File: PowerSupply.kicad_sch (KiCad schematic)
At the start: 8 parts, among them U301 TPSM33625

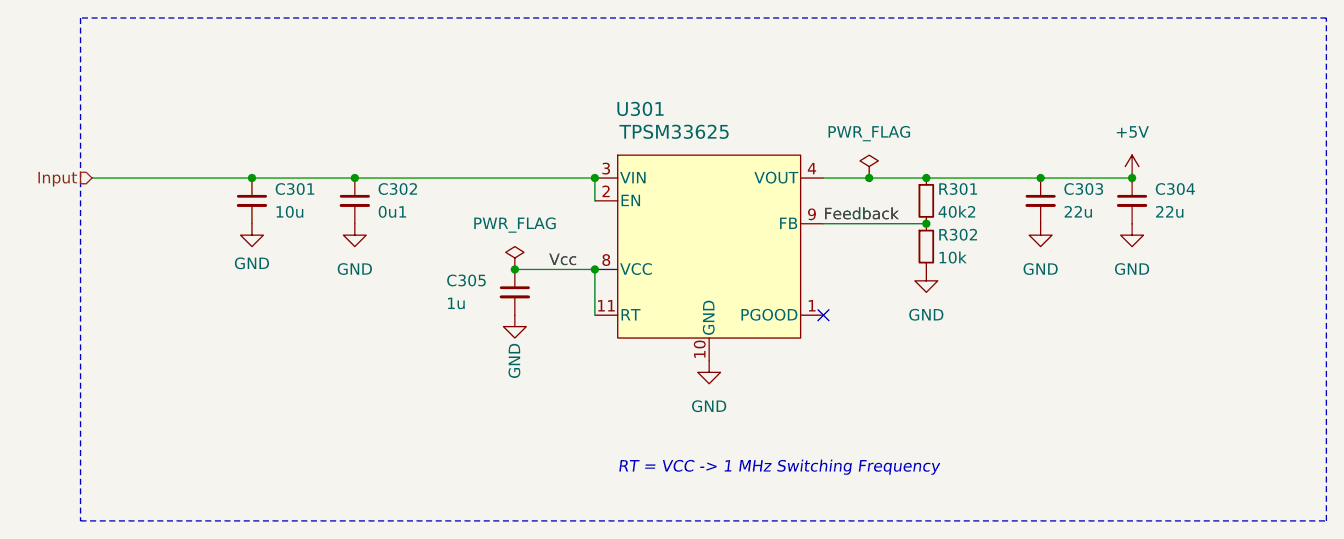
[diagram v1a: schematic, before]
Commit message: Update DCDC
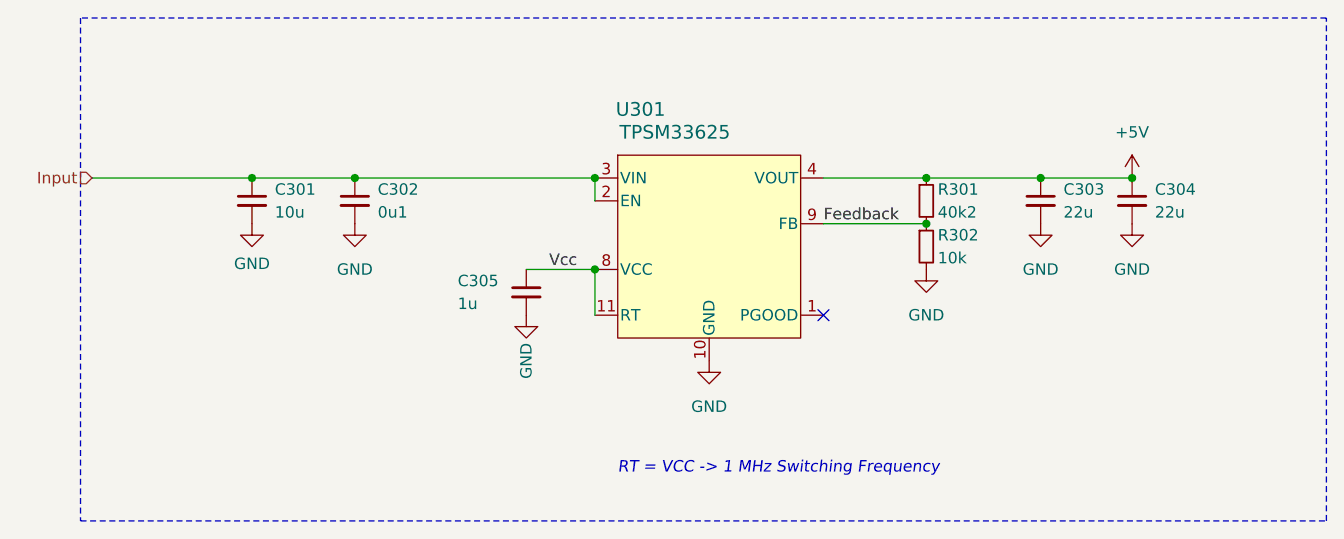
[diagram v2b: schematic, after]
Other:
- moved on the sheet: C305
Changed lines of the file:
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@@
 	(title_block
 		(title "Power Supply")
-		(date "2023-08-08")
-		(rev "3")
+		(date "2024-03-28")
+		(rev "4")
 		(company "+5V")
-	)
-	(junction
-		(at 166.37 95.25)
-		(diameter 0)
-		(color 0 0 0 0)
-	)
-	(junction
-		(at 127 105.41)
-		(diameter 0)
-		(color 0 0 0 0)
 	)
 	(junction
@@
 	(wire
 		(pts
-			(xy 127 105.41) (xy 135.89 105.41)
+			(xy 128.27 105.41) (xy 135.89 105.41)
 		)
 		(stroke
@@
 	(wire
 		(pts
-			(xy 166.37 95.25) (xy 172.72 95.25)
+			(xy 172.72 95.25) (xy 185.42 95.25)
 		)
 		(stroke
@@
 		)
 	)
+	(polyline
+		(pts
+			(xy 217.17 77.47) (xy 78.74 77.47)
+		)
+		(stroke
+			(width 0)
+			(type dash)
+		)
+	)
 	(wire
 		(pts
-			(xy 172.72 95.25) (xy 185.42 95.25)
-		)
-		(stroke
-			(width 0)
-			(type default)
-		)
-	)
-	(polyline
-		(pts
-			(xy 217.17 77.47) (xy 78.74 77.47)
-		)
-		(stroke
-			(width 0)
-			(type dash)
-		)
-	)
-	(wire
-		(pts
-			(xy 161.29 95.25) (xy 166.37 95.25)
+			(xy 161.29 95.25) (xy 172.72 95.25)
 		)
 		(stroke
@@
 	)
 	(symbol
-		(lib_id "power:PWR_FLAG")
-		(at 166.37 95.25 0)
-		(unit 1)
-		(exclude_from_sim no)
-		(in_bom yes)
-		(on_board yes)
-		(dnp no)
-		(fields_autoplaced yes)
-		(property "Reference" "#FLG0301"
-			(at 166.37 93.345 0)
-			(effects
-				(font
-					(size 1.27 1.27)
-				)
-				(hide yes)
-			)
-		)
-		(property "Value" "PWR_FLAG"
-			(at 166.37 90.17 0)
-			(effects
-				(font
-					(size 1.27 1.27)
-				)
-			)
-		)
-		(property "Footprint" ""
-			(at 166.37 95.25 0)
-			(effects
-				(font
-					(size 1.27 1.27)
-				)
-				(hide yes)
-			)
-		)
-		(property "Datasheet" "~"
-			(at 166.37 95.25 0)
-			(effects
-				(font
-					(size 1.27 1.27)
-				)
-				(hide yes)
-			)
-		)
-		(property "Description" ""
-			(at 166.37 95.25 0)
-			(effects
-				(font
-					(size 1.27 1.27)
-				)
-				(hide yes)
-			)
-		)
-		(pin "1"
-		)
-		(instances
-			(project "power-rj45"
-				(path "/6c8448b4-b04d-47e1-934e-e40cbe27a7be/24a9dc0c-cb3c-464a-a734-f09bf949d71a"
-					(reference "#FLG0301")
-					(unit 1)
-				)
-			)
-		)
-	)
-	(symbol
 		(lib_id "V2_Converter_DCDC:TPSM33625")
 		(at 148.59 102.87 0)
@@
 	(symbol
 		(lib_id "Device:C_Small")
-		(at 127 107.95 0)
+		(at 128.27 107.95 0)
 		(unit 1)
 		(exclude_from_sim no)
@@
 		(dnp no)
 		(property "Reference" "C305"
-			(at 119.38 106.68 0)
+			(at 120.65 106.68 0)
 			(effects
 				(font
@@
 		)
 		(property "Value" "1u"
-			(at 119.38 109.22 0)
+			(at 120.65 109.22 0)
 			(effects
 				(font
@@
 		)
 		(property "Footprint" "Capacitor_SMD:C_0603_1608Metric"
-			(at 127 107.95 0)
+			(at 128.27 107.95 0)
 			(effects
 				(font
@@
 		)
 		(property "Datasheet" "~"
-			(at 127 107.95 0)
-			(effects
-				(font
-					(size 1.27 1.27)
-				)
-				(hide yes)
-			)
-		)
-		(property "Description" ""
-			(at 127 107.95 0)
+			(at 128.27 107.95 0)
+			(effects
+				(font
+					(size 1.27 1.27)
+				)
+				(hide yes)
+			)
+		)
+		(property "Description" ""
+			(at 128.27 107.95 0)
 			(effects
 				(font
@@
 	(symbol
 		(lib_id "power:GND")
-		(at 127 110.49 0)
+		(at 128.27 110.49 0)
 		(unit 1)
 		(exclude_from_sim no)
@@
 		(dnp no)
 		(property "Reference" "#PWR0307"
-			(at 127 116.84 0)
+			(at 128.27 116.84 0)
 			(effects
 				(font
@@
 		)
 		(property "Value" "GND"
-			(at 127 115.57 90)
+			(at 128.27 115.57 90)
 			(effects
 				(font
@@
 		)
 		(property "Footprint" ""
-			(at 127 110.49 0)
+			(at 128.27 110.49 0)
 			(effects
 				(font
@@
 		)
 		(property "Datasheet" ""
-			(at 127 110.49 0)
-			(effects
-				(font
-					(size 1.27 1.27)
-				)
-				(hide yes)
-			)
-		)
-		(property "Description" ""
-			(at 127 110.49 0)
+			(at 128.27 110.49 0)
+			(effects
+				(font
+					(size 1.27 1.27)
+				)
+				(hide yes)
+			)
+		)
+		(property "Description" ""
+			(at 128.27 110.49 0)
 			(effects
 				(font
@@
 					(unit 1)
 				)
-			)
-		)
-	)
-	(symbol
-		(lib_id "power:PWR_FLAG")
-		(at 127 105.41 0)
-		(unit 1)
-		(exclude_from_sim no)
-		(in_bom yes)
-		(on_board yes)
-		(dnp no)
-		(fields_autoplaced yes)
-		(property "Reference" "#FLG0302"
-			(at 127 103.505 0)
-			(effects
-				(font
-					(size 1.27 1.27)
-				)
-				(hide yes)
-			)
-		)
-		(property "Value" "PWR_FLAG"
-			(at 127 100.33 0)
-			(effects
-				(font
-					(size 1.27 1.27)
-				)
-			)
-		)
-		(property "Footprint" ""
-			(at 127 105.41 0)
-			(effects
-				(font
-					(size 1.27 1.27)
-				)
-				(hide yes)
-			)
-		)
-		(property "Datasheet" "~"
-			(at 127 105.41 0)
-			(effects
-				(font
-					(size 1.27 1.27)
-				)
-				(hide yes)
-			)
-		)
-		(property "Description" ""
-			(at 127 105.41 0)
-			(effects
-				(font
-					(size 1.27 1.27)
-				)
-				(hide yes)
-			)
-		)
-		(pin "1"
-		)
-		(instances
-			(project "power-rj45"
-				(path "/6c8448b4-b04d-47e1-934e-e40cbe27a7be/24a9dc0c-cb3c-464a-a734-f09bf949d71a"
-					(reference "#FLG0302")
-					(unit 1)
-				)

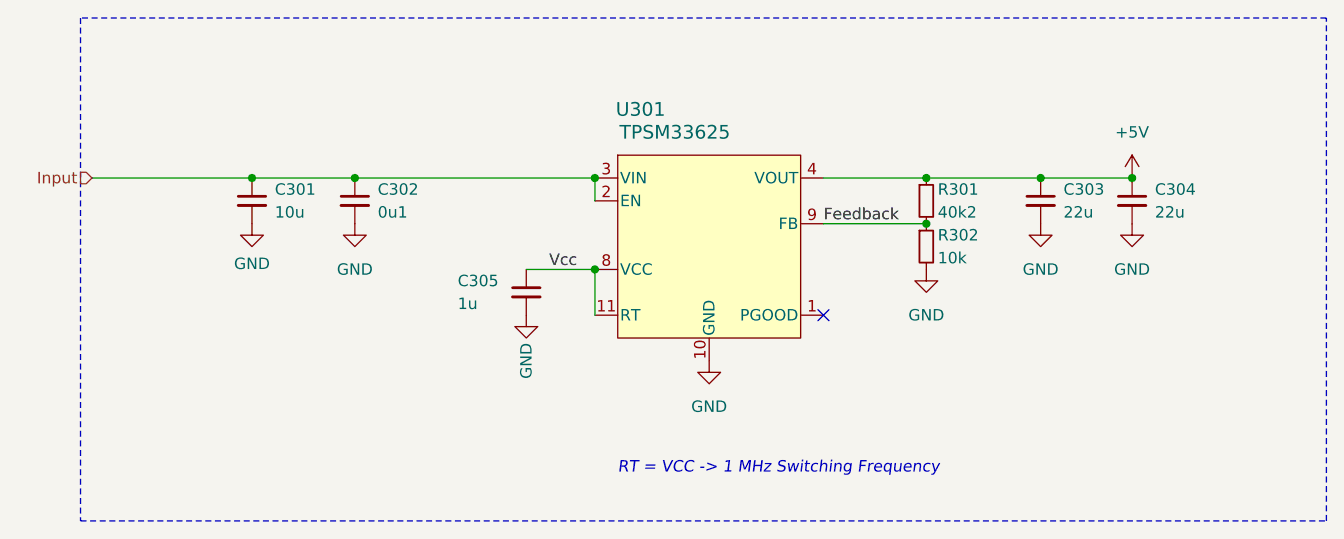
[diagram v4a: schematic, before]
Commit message: Resize to 70 mm
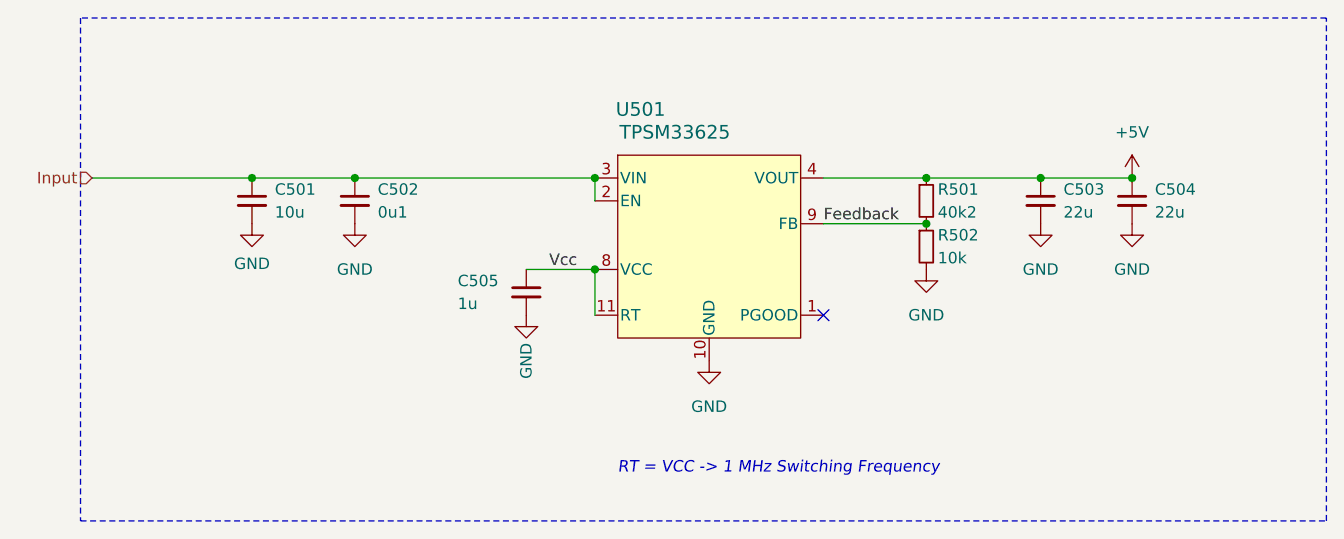
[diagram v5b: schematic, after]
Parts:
- renumbered C301 to C501, C302 to C502, C303 to C503, C304 to C504, C305 to C505, R301 to R501, R302 to R502, U301 to U501
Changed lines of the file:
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@@
 		(on_board yes)
 		(dnp no)
-		(property "Reference" "U301"
+		(property "Reference" "U501"
 			(at 140.97 87.63 0)
 			(effects
@@
 			(project "power-rj45"
 				(path "/6c8448b4-b04d-47e1-934e-e40cbe27a7be/24a9dc0c-cb3c-464a-a734-f09bf949d71a"
-					(reference "U301")
+					(reference "U501")
 					(unit 1)
 				)
@@
 		(on_board yes)
 		(dnp no)
-		(property "Reference" "C302"
+		(property "Reference" "C502"
 			(at 111.76 96.52 0)
 			(effects
@@
 			(project "power-rj45"
 				(path "/6c8448b4-b04d-47e1-934e-e40cbe27a7be/24a9dc0c-cb3c-464a-a734-f09bf949d71a"
-					(reference "C302")
+					(reference "C502")
 					(unit 1)
 				)
@@
 		(on_board yes)
 		(dnp no)
-		(property "Reference" "C304"
+		(property "Reference" "C504"
 			(at 198.12 96.52 0)
 			(effects
@@
 			(project "power-rj45"
 				(path "/6c8448b4-b04d-47e1-934e-e40cbe27a7be/24a9dc0c-cb3c-464a-a734-f09bf949d71a"
-					(reference "C304")
+					(reference "C504")
 					(unit 1)
 				)
@@
 		(on_board yes)
 		(dnp no)
-		(property "Reference" "R301"
+		(property "Reference" "R501"
 			(at 173.99 96.52 0)
 			(effects
@@
 			(project "power-rj45"
 				(path "/6c8448b4-b04d-47e1-934e-e40cbe27a7be/24a9dc0c-cb3c-464a-a734-f09bf949d71a"
-					(reference "R301")
+					(reference "R501")
 					(unit 1)
 				)
@@
 		(on_board yes)
 		(dnp no)
-		(property "Reference" "#PWR0304"
+		(property "Reference" "#PWR0504"
 			(at 185.42 106.68 0)
 			(effects
@@
 			(project "power-rj45"
 				(path "/6c8448b4-b04d-47e1-934e-e40cbe27a7be/24a9dc0c-cb3c-464a-a734-f09bf949d71a"
-					(reference "#PWR0304")
+					(reference "#PWR0504")
 					(unit 1)
 				)
@@
 		(on_board yes)
 		(dnp no)
-		(property "Reference" "#PWR0305"
+		(property "Reference" "#PWR0505"
 			(at 195.58 106.68 0)
 			(effects
@@
 			(project "power-rj45"
 				(path "/6c8448b4-b04d-47e1-934e-e40cbe27a7be/24a9dc0c-cb3c-464a-a734-f09bf949d71a"
-					(reference "#PWR0305")
+					(reference "#PWR0505")
 					(unit 1)
 				)
@@
 		(on_board yes)
 		(dnp no)
-		(property "Reference" "#PWR0301"
+		(property "Reference" "#PWR0501"
 			(at 195.58 99.06 0)
 			(effects
@@
 			(project "power-rj45"
 				(path "/6c8448b4-b04d-47e1-934e-e40cbe27a7be/24a9dc0c-cb3c-464a-a734-f09bf949d71a"
-					(reference "#PWR0301")
+					(reference "#PWR0501")
 					(unit 1)
 				)
@@
 		(on_board yes)
 		(dnp no)
-		(property "Reference" "#PWR0302"
+		(property "Reference" "#PWR0502"
 			(at 97.79 106.68 0)
 			(effects
@@
 			(project "power-rj45"
 				(path "/6c8448b4-b04d-47e1-934e-e40cbe27a7be/24a9dc0c-cb3c-464a-a734-f09bf949d71a"
-					(reference "#PWR0302")
+					(reference "#PWR0502")
 					(unit 1)
 				)
@@
 		(on_board yes)
 		(dnp no)
-		(property "Reference" "#PWR0306"
+		(property "Reference" "#PWR0506"
 			(at 172.72 111.76 0)
 			(effects
@@
 			(project "power-rj45"
 				(path "/6c8448b4-b04d-47e1-934e-e40cbe27a7be/24a9dc0c-cb3c-464a-a734-f09bf949d71a"
-					(reference "#PWR0306")
+					(reference "#PWR0506")
 					(unit 1)
 				)
@@
 		(on_board yes)
 		(dnp no)
-		(property "Reference" "#PWR0303"
+		(property "Reference" "#PWR0503"
 			(at 109.22 106.68 0)
 			(effects
@@
 			(project "power-rj45"
 				(path "/6c8448b4-b04d-47e1-934e-e40cbe27a7be/24a9dc0c-cb3c-464a-a734-f09bf949d71a"
-					(reference "#PWR0303")
+					(reference "#PWR0503")
 					(unit 1)
 				)
@@
 		(on_board yes)
 		(dnp no)
-		(property "Reference" "C305"
+		(property "Reference" "C505"
 			(at 120.65 106.68 0)
 			(effects
@@
 			(project "power-rj45"
 				(path "/6c8448b4-b04d-47e1-934e-e40cbe27a7be/24a9dc0c-cb3c-464a-a734-f09bf949d71a"
-					(reference "C305")
+					(reference "C505")
 					(unit 1)
 				)
@@
 		(on_board yes)
 		(dnp no)
-		(property "Reference" "C303"
+		(property "Reference" "C503"
 			(at 187.96 96.52 0)
 			(effects
@@
 			(project "power-rj45"
 				(path "/6c8448b4-b04d-47e1-934e-e40cbe27a7be/24a9dc0c-cb3c-464a-a734-f09bf949d71a"
-					(reference "C303")
+					(reference "C503")
 					(unit 1)
 				)
@@
 		(on_board yes)
 		(dnp no)
-		(property "Reference" "#PWR0307"
+		(property "Reference" "#PWR0507"
 			(at 128.27 116.84 0)
 			(effects
@@
 			(project "power-rj45"
 				(path "/6c8448b4-b04d-47e1-934e-e40cbe27a7be/24a9dc0c-cb3c-464a-a734-f09bf949d71a"
-					(reference "#PWR0307")
+					(reference "#PWR0507")
 					(unit 1)
 				)
@@
 		(on_board yes)
 		(dnp no)
-		(property "Reference" "R302"
+		(property "Reference" "R502"
 			(at 173.99 101.6 0)
 			(effects
@@
 			(project "power-rj45"
 				(path "/6c8448b4-b04d-47e1-934e-e40cbe27a7be/24a9dc0c-cb3c-464a-a734-f09bf949d71a"
-					(reference "R302")
+					(reference "R502")
 					(unit 1)
 				)
@@
 		(on_board yes)
 		(dnp no)
-		(property "Reference" "#PWR0308"
+		(property "Reference" "#PWR0508"
 			(at 148.59 121.92 0)
 			(effects
@@
 			(project "power-rj45"
 				(path "/6c8448b4-b04d-47e1-934e-e40cbe27a7be/24a9dc0c-cb3c-464a-a734-f09bf949d71a"
-					(reference "#PWR0308")
+					(reference "#PWR0508")
 					(unit 1)
 				)
@@
 		(on_board yes)
 		(dnp no)
-		(property "Reference" "C301"
+		(property "Reference" "C501"
 			(at 100.33 96.52 0)
 			(effects
@@
 			(project "power-rj45"
 				(path "/6c8448b4-b04d-47e1-934e-e40cbe27a7be/24a9dc0c-cb3c-464a-a734-f09bf949d71a"
-					(reference "C301")
-					(unit 1)
-				)
+					(reference "C501")
+					(unit 1)
+				)

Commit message: GND label
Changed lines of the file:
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@@
 					(size 1.27 1.27)
 				)
+				(hide yes)
 			)
 		)
@@
 					(size 1.27 1.27)
 				)
+				(hide yes)
 			)
 		)
@@
 					(size 1.27 1.27)
 				)
+				(hide yes)
 			)
 		)
@@
 					(size 1.27 1.27)
 				)
+				(hide yes)
 			)
 		)
@@
 					(size 1.27 1.27)
 				)
+				(hide yes)
 			)
 		)
@@
 					(size 1.27 1.27)
 				)
+				(hide yes)
 			)
 		)
@@
 					(size 1.27 1.27)
 				)
-			)
-		)
+				(hide yes)
+			)
+		)
